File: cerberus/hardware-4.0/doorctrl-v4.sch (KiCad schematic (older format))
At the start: 7 parts, among them CON1 AVR-ISP-6, CON2 AVR-JTAG-10, IC1 ATMEGA324P-A, U8 24LC64, X1 20 MHz

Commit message: Fixed atmel lib to not floodfill
git-svn-id: file:///home/ff/projects/osaa/svn@221 a092026d-3e22-4cff-94a7-eaa6fdd35d37
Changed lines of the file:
@@
-EESchema Schematic File Version 2  date 2010-12-18T14:25:32 CET
+EESchema Schematic File Version 2  date 2010-12-18T14:49:05 CET
 LIBS:enc28j60
 LIBS:power
@@
 LIBS:siliconi
 LIBS:opto
-LIBS:atmel
 LIBS:contrib
 LIBS:valves
@@
 LIBS:i2c
 LIBS:linear
+LIBS:atmel
 LIBS:doorctrl-v4-cache
 EELAYER 24  0
@@
 Sheet 1 6
 Title ""
-Date "17 dec 2010"
+Date "18 dec 2010"
 Rev ""
 Comp ""
@@
 	3300 850  3300 775
 Wire Wire Line
-	3300 775  2800 775
+	3300 775  3125 775
+Wire Wire Line
+	3125 775  3000 775
+Wire Wire Line
+	3000 775  2900 775
+Wire Wire Line
+	2900 775  2800 775
 Wire Wire Line
 	2800 775  2800 850
@@
 	3200 4850 3200 4950
 Wire Wire Line
-	3200 4950 2900 4950
+	3200 4950 3100 4950
+Wire Wire Line
+	3100 4950 3050 4950
+Wire Wire Line
+	3050 4950 3000 4950
+Wire Wire Line
+	3000 4950 2900 4950
 Wire Wire Line
 	2900 4950 2900 4850
@@
 Connection ~ 2100 1950
 Wire Wire Line
-	1750 1950 2150 1950
+	1750 1950 1850 1950
+Wire Wire Line
+	1850 1950 2100 1950
+Wire Wire Line
+	2100 1950 2150 1950
 Connection ~ 1850 1950
 Wire Wire Line
@@
 	1750 3425 1750 3525
 Wire Wire Line
-	2600 6825 2600 6275
+	2600 6825 2600 6475
+Wire Wire Line
+	2600 6475 2600 6375
+Wire Wire Line
+	2600 6375 2600 6275
 Connection ~ 2600 6475
 Wire Wire Line

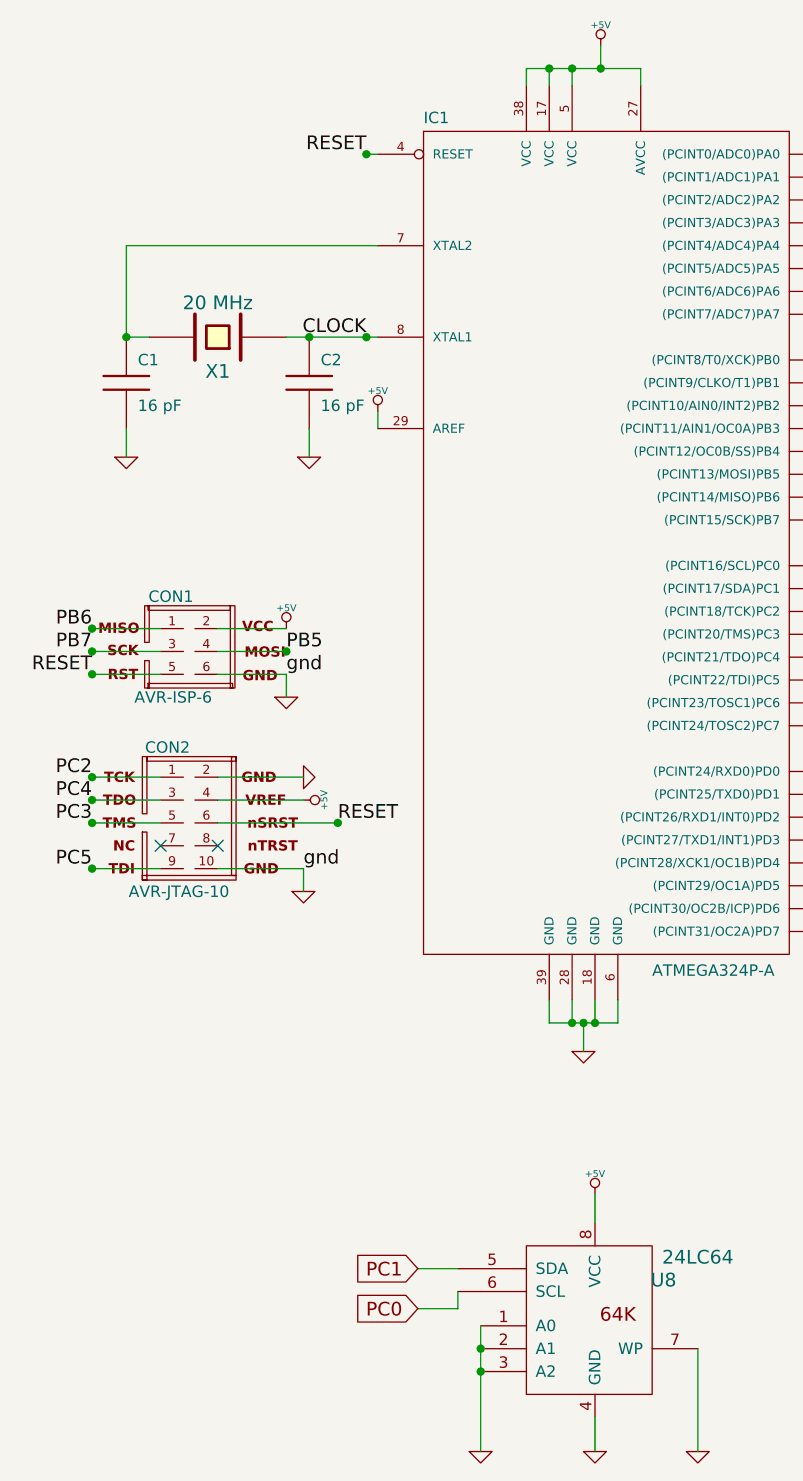
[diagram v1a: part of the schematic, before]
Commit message: Added torroid coil and proper diode packages
git-svn-id: file:///home/ff/projects/osaa/svn@222 a092026d-3e22-4cff-94a7-eaa6fdd35d37
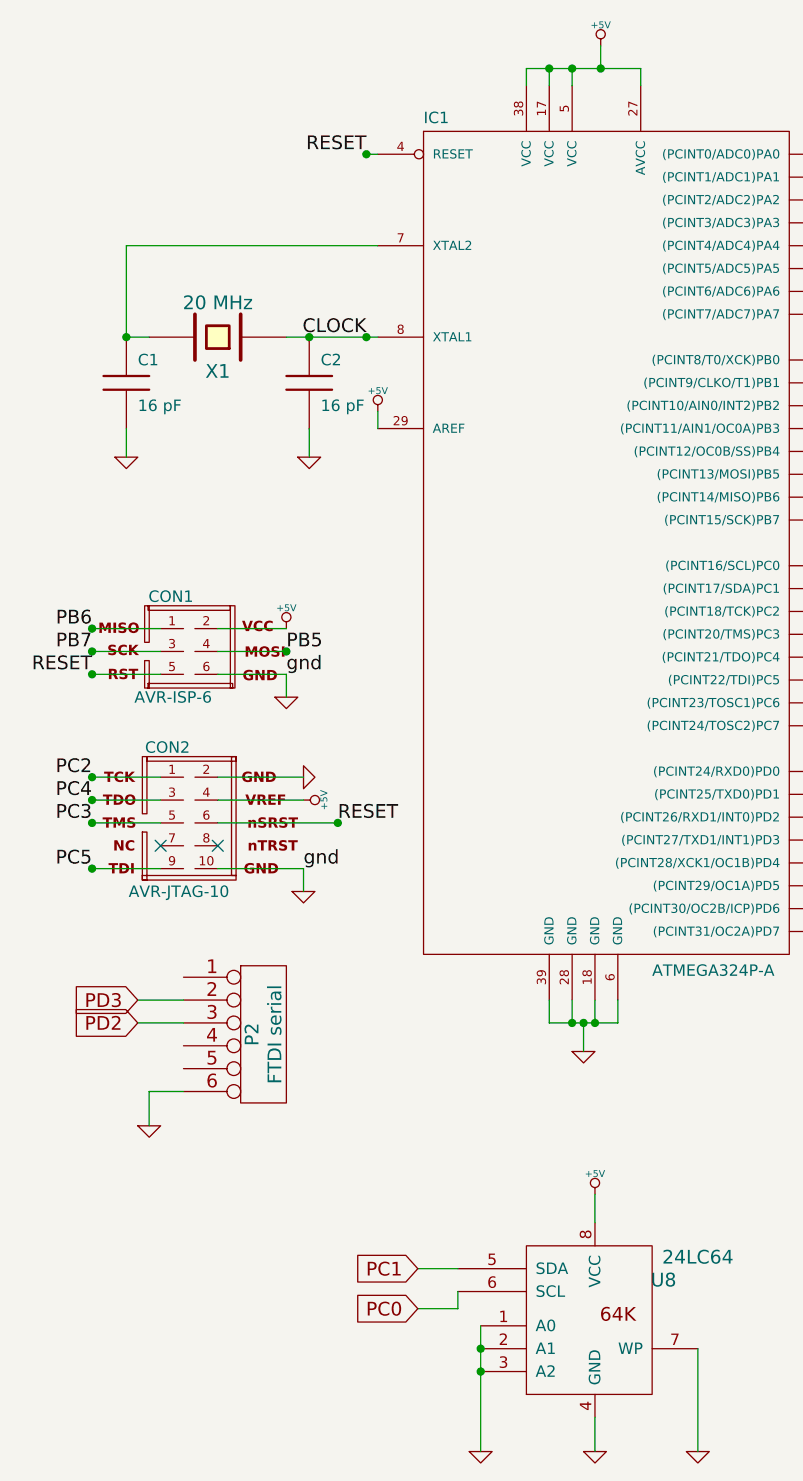
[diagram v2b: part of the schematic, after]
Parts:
- added P2: FTDI serial, symbol CONN_6
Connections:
- net GND: now also P2.6
- net PD2: now also P2.3
- net PD3: now also P2.2

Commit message: Converted to 2010-12-18
git-svn-id: file:///home/ff/projects/osaa/svn@225 a092026d-3e22-4cff-94a7-eaa6fdd35d37
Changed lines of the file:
@@
-EESchema Schematic File Version 2  date 2010-12-20T22:26:04 CET
+EESchema Schematic File Version 2  date 2010-12-21T17:47:20 CET
 LIBS:enc28j60
 LIBS:power
@@
 Sheet 1 6
 Title ""
-Date "20 dec 2010"
+Date "21 dec 2010"
 Rev ""
 Comp ""
@@
 Comment4 ""
 $EndDescr
+$Sheet
+S 9300 2100 1600 1000
+U 4CFD2FB8
+F0 "doorctrl-v4-net" 60
+F1 "doorctrl-v4-net.sch" 60
+F2 "SCK" I L 9300 2250 60
+F3 "MISO" O L 9300 2400 60
+F4 "MOSI" I L 9300 2550 60
+F5 "~CS" I L 9300 2700 60
+F6 "Clock-out" O L 9300 2850 60
+$EndSheet
 Wire Wire Line
 	1300 4850 1100 4850
@@
 $EndComp
 $Sheet
-S 9300 2100 1600 1000
-U 4CFD2FB8
-F0 "doorctrl-v4-net" 60
-F1 "doorctrl-v4-net.sch" 60
-F2 "SCK" I L 9300 2250 60
-F3 "MISO" O L 9300 2400 60
-F4 "MOSI" I L 9300 2550 60
-F5 "~CS" I L 9300 2700 60
-F6 "Clock out" O L 9300 2850 60
-$EndSheet
-$Sheet
 S 9300 5025 1625 850

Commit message: Finished the copper layers
git-svn-id: file:///home/ff/projects/osaa/svn@229 a092026d-3e22-4cff-94a7-eaa6fdd35d37
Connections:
- net CLOCK: no longer names the net of C2.1, IC1.8 (XTAL1), X1.1
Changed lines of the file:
@@
-EESchema Schematic File Version 2  date 2010-12-21T17:47:20 CET
+EESchema Schematic File Version 2  date 2010-12-23T21:46:15 CET
 LIBS:enc28j60
 LIBS:power
@@
 LIBS:diode
 LIBS:doorctrl-v4-cache
-EELAYER 24  0
+EELAYER 25  0
 EELAYER END
 $Descr A4 11700 8267
 Sheet 1 6
 Title ""
-Date "21 dec 2010"
+Date "23 dec 2010"
 Rev ""
 Comp ""
@@
 F4 "MOSI" I L 9300 2550 60
 F5 "~CS" I L 9300 2700 60
-F6 "Clock-out" O L 9300 2850 60
 $EndSheet
 Wire Wire Line
@@
 Wire Wire Line
 	9100 4075 9325 4075
-Wire Wire Line
-	9300 2850 9100 2850
 Wire Wire Line
 	9300 2550 9100 2550
@@
 Text GLabel 9100 3875 0    60   Input ~ 0
 PB1
-Text GLabel 9100 2850 0    60   Input ~ 0
-CLOCK
 Text GLabel 9100 2700 0    60   Input ~ 0
 PB4
@@
 Text Label 4225 2950 0    60   ~ 0
 PC0
-Text Label 2100 1950 2    60   ~ 0
-CLOCK
 Text Label 2100 1150 2    60   ~ 0
 RESET

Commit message: Various tweakage
git-svn-id: file:///home/ff/projects/osaa/svn@233 a092026d-3e22-4cff-94a7-eaa6fdd35d37
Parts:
- added P3: 5x2 header, symbol CONN_5X2
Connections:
- net +5V: now also P3.2
- net GND: now also P3.4
- net PB0: now also P3.7
- net PB2: now also P3.8
- net PB3: now also P3.9
- net PB4: now also P3.10
- net PC0: now also P3.5
- net PC1: now also P3.6
- new net +12V: P3.1
- new net +3.3V: P3.3
- no-connect marks 2 -> 5
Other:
- note added: "Extension header"
- moved on the sheet: U8

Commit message: Misc changes
git-svn-id: file:///home/ff/projects/osaa/svn@234 a092026d-3e22-4cff-94a7-eaa6fdd35d37
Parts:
- added R63, R64: 1k, symbol R
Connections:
- net +5V: now also R63.1, R64.1
- net PC0: now also R63.2
- net PC1: now also R64.2
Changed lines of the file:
@@
-EESchema Schematic File Version 2  date 2010-12-27T14:47:10 CET
+EESchema Schematic File Version 2  date 2010-12-28T16:33:17 CET
 LIBS:enc28j60
 LIBS:power
@@
 Sheet 1 6
 Title ""
-Date "27 dec 2010"
+Date "28 dec 2010"
 Rev ""
 Comp ""
@@
 Comment4 ""
 $EndDescr
-Wire Wire Line
-	3850 6125 3675 6125
+$Comp
+L +5V #PWR?
+U 1 1 4D1A0335
+P 3600 5300
+F 0 "#PWR?" H 3600 5390 20  0001 C CNN
+F 1 "+5V" H 3600 5390 30  0000 C CNN
+	1    3600 5300
+	1    0    0    -1
+$EndComp
+Wire Wire Line
+	3275 6125 3850 6125
+Wire Wire Line
+	3850 6025 3275 6025
+Connection ~ 3500 6125
+Wire Wire Line
+	3500 6125 3500 5925
+Connection ~ 3600 5350
+Wire Wire Line
+	3600 5350 3600 5300
 Wire Wire Line
 	2100 6325 2050 6325
@@
 	4900 6825 4900 6375
 Wire Wire Line
-	3850 6025 3675 6025
-Wire Wire Line
 	9100 2250 9300 2250
 Wire Wire Line
@@
 Wire Wire Line
 	2050 6425 2100 6425
+Wire Wire Line
+	3500 5425 3500 5350
+Wire Wire Line
+	3500 5350 3700 5350
+Wire Wire Line
+	3700 5350 3700 5425
+Wire Wire Line
+	3700 6025 3700 5925
+Connection ~ 3700 6025
+$Comp
+L R R63
+U 1 1 4D1A01F5
+P 3500 5675
+F 0 "R63" V 3580 5675 50  0000 C CNN
+F 1 "1k" V 3500 5675 50  0000 C CNN
+	1    3500 5675
+	1    0    0    -1
+$EndComp
+$Comp
+L R R64
+U 1 1 4D1A01EA
+P 3700 5675
+F 0 "R64" V 3780 5675 50  0000 C CNN
+F 1 "1k" V 3700 5675 50  0000 C CNN
+	1    3700 5675
+	1    0    0    -1
+$EndComp
 Text Notes 1300 6625 0    60   ~ 0
 Extension header
@@
 PD3
 $Comp
-L GND #PWR01
+L GND #PWR02
 U 1 1 4D0D1ABE
 P 1150 5400
-F 0 "#PWR01" H 1150 5400 30  0001 C CNN
+F 0 "#PWR02" H 1150 5400 30  0001 C CNN
 F 1 "GND" H 1150 5330 30  0001 C CNN
 	1    1150 5400
@@
 PB7
 $Comp
-L +5V #PWR02
+L +5V #PWR03
 U 1 1 4D0BBC2E
 P 2150 2275
-F 0 "#PWR02" H 2150 2365 20  0001 C CNN
+F 0 "#PWR03" H 2150 2365 20  0001 C CNN
 F 1 "+5V" H 2150 2365 30  0000 C CNN
 	1    2150 2275
 	1    0    0    -1
 $EndComp
-Text GLabel 3675 6125 0    60   Input ~ 0
+Text GLabel 3275 6125 0    60   Input ~ 0
 PC0
-Text GLabel 3675 6025 0    60   Input ~ 0
+Text GLabel 3275 6025 0    60   Input ~ 0
 PC1
 $Comp
-L +5V #PWR03
+L +5V #PWR04
 U 1 1 4D0BB852
 P 4450 5700
-F 0 "#PWR03" H 4450 5790 20  0001 C CNN
+F 0 "#PWR04" H 4450 5790 20  0001 C CNN
 F 1 "+5V" H 4450 5790 30  0000 C CNN
 	1    4450 5700
@@
 $EndComp
 $Comp
-L GND #PWR04
+L GND #PWR05
 U 1 1 4D0BB830
 P 3950 6825
-F 0 "#PWR04" H 3950 6825 30  0001 C CNN
+F 0 "#PWR05" H 3950 6825 30  0001 C CNN
 F 1 "GND" H 3950 6755 30  0001 C CNN
 	1    3950 6825
@@
 $EndComp
 $Comp
-L GND #PWR05
+L GND #PWR06
 U 1 1 4D0BB82C
 P 4450 6825
-F 0 "#PWR05" H 4450 6825 30  0001 C CNN
+F 0 "#PWR06" H 4450 6825 30  0001 C CNN
 F 1 "GND" H 4450 6755 30  0001 C CNN
 	1    4450 6825
@@
 $EndComp
 $Comp
-L GND #PWR06
+L GND #PWR07
 U 1 1 4D0BB822
 P 4900 6825
-F 0 "#PWR06" H 4900 6825 30  0001 C CNN
+F 0 "#PWR07" H 4900 6825 30  0001 C CNN
 F 1 "GND" H 4900 6755 30  0001 C CNN
 	1    4900 6825
@@
 $EndSheet
 $Comp
-L GND #PWR07
+L GND #PWR08
 U 1 1 4D0BAF81
 P 1825 3875
-F 0 "#PWR07" H 1825 3875 30  0001 C CNN
+F 0 "#PWR08" H 1825 3875 30  0001 C CNN
 F 1 "GND" H 1825 3805 30  0001 C CNN
 	1    1825 3875
@@
 $EndComp
 $Comp
-L +5V #PWR08
+L +5V #PWR09
 U 1 1 4D0BAF77
 P 1825 3975
-F 0 "#PWR08" H 1825 4065 20  0001 C CNN
+F 0 "#PWR09" H 1825 4065 20  0001 C CNN
 F 1 "+5V" H 1825 4065 30  0000 C CNN
 	1    1825 3975
@@
 $EndComp
 $Comp
-L GND #PWR09
+L GND #PWR010
 U 1 1 4D0BAF62
 P 1825 4375
-F 0 "#PWR09" H 1825 4375 30  0001 C CNN
+F 0 "#PWR010" H 1825 4375 30  0001 C CNN
 F 1 "GND" H 1825 4305 30  0001 C CNN
 	1    1825 4375
@@
 $EndComp
 $Comp
-L GND #PWR010
+L GND #PWR011
 U 1 1 4D0BAF4F
 P 1750 3525
-F 0 "#PWR010" H 1750 3525 30  0001 C CNN
+F 0 "#PWR011" H 1750 3525 30  0001 C CNN
 F 1 "GND" H 1750 3455 30  0001 C CNN
 	1    1750 3525
@@
 $EndComp
 $Comp
-L +5V #PWR011
+L +5V #PWR012
 U 1 1 4D0BAF48
 P 1750 3225
-F 0 "#PWR011" H 1750 3315 20  0001 C CNN
+F 0 "#PWR012" H 1750 3315 20  0001 C CNN
 F 1 "+5V" H 1750 3315 30  0000 C CNN
 	1    1750 3225
@@
 $EndComp
 $Comp
-L +5V #PWR012
+L +5V #PWR013
 U 1 1 4D0BAF41
 P 3125 675
-F 0 "#PWR012" H 3125 765 20  0001 C CNN
+F 0 "#PWR013" H 3125 765 20  0001 C CNN
 F 1 "+5V" H 3125 765 30  0000 C CNN
 	1    3125 675
@@
 PB5
 $Comp
-L GND #PWR013
+L GND #PWR014
 U 1 1 4CFAB0A0
 P 1850 2475
-F 0 "#PWR013" H 1850 2475 30  0001 C CNN
+F 0 "#PWR014" H 1850 2475 30  0001 C CNN
 F 1 "GND" H 1850 2405 30  0001 C CNN
 	1    1850 2475
@@
 $EndComp
 $Comp
-L GND #PWR014
+L GND #PWR015
 U 1 1 4CFAB098
 P 1050 2475
-F 0 "#PWR014" H 1050 2475 30  0001 C CNN
+F 0 "#PWR015" H 1050 2475 30  0001 C CNN
 F 1 "GND" H 1050 2405 30  0001 C CNN
 	1    1050 2475
@@
 RESET
 $Comp
-L GND #PWR015
+L GND #PWR016
 U 1 1 4CF6BFD7
 P 3050 5075
-F 0 "#PWR015" H 3050 5075 30  0001 C CNN
+F 0 "#PWR016" H 3050 5075 30  0001 C CNN
 F 1 "GND" H 3050 5005 30  0001 C CNN
 	1    3050 5075
